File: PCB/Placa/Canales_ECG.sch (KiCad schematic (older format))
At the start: 39 parts, among them U1 INA333, U2 OPA2335, U3 OPA2335, U6 INA333, U7 OPA2335, U8 OPA2335

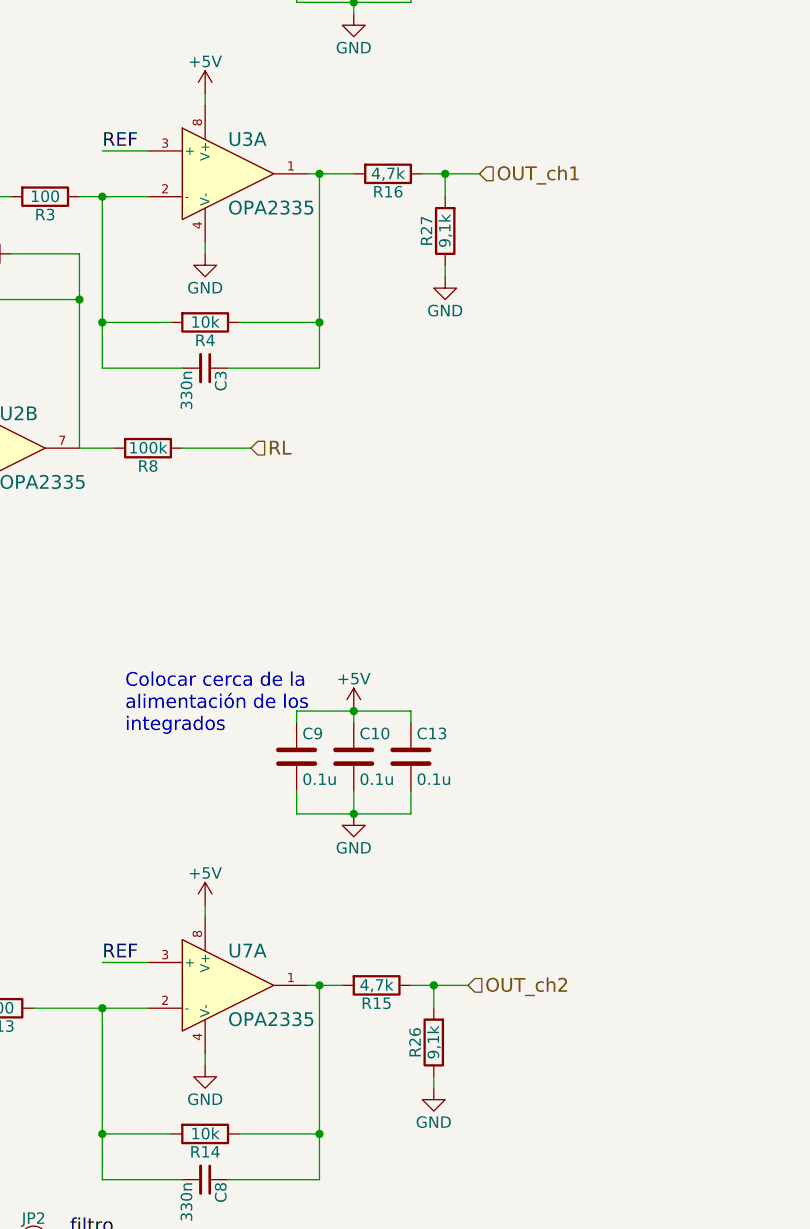
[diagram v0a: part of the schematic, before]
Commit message: Recalculé unas resistencias porque consigo de la serie E12
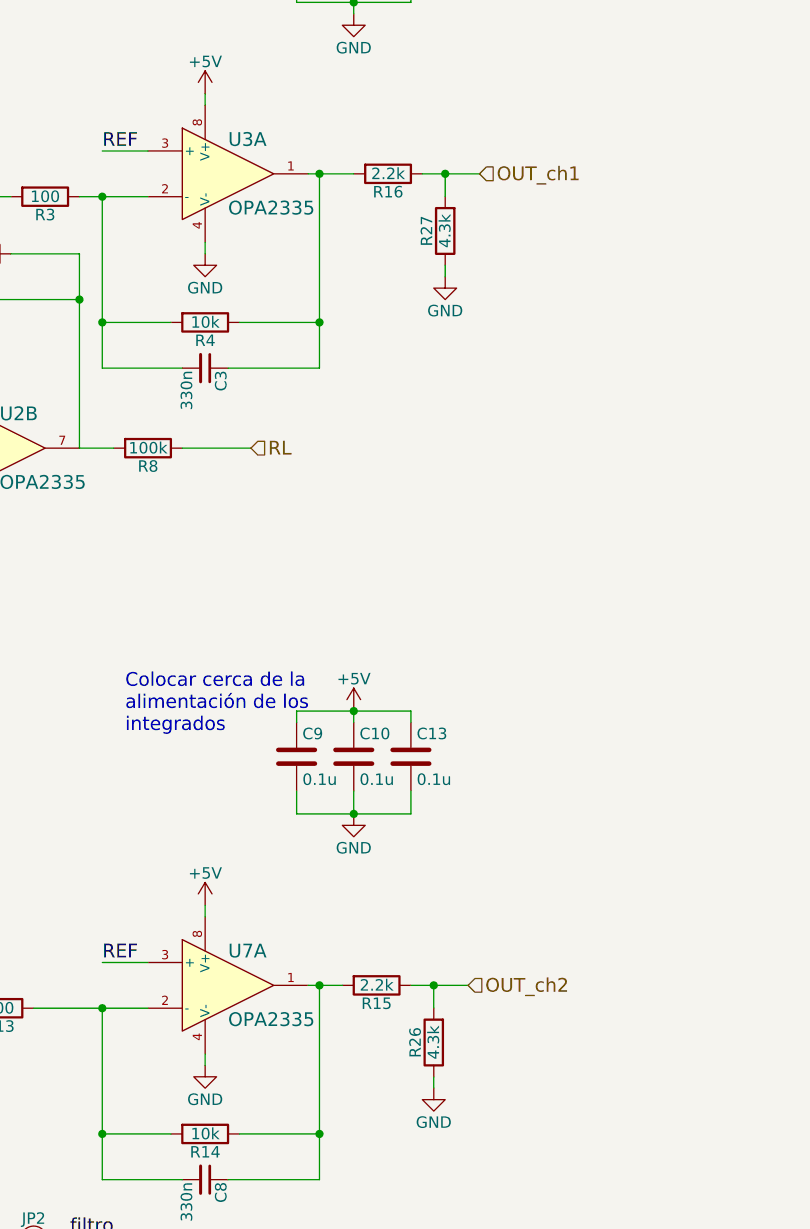
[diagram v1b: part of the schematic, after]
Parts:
- R15, R16: value 4,7k -> 2.2k
- R26, R27: value 9,1k -> 4.3k
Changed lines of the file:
@@
 P 5550 2050
 F 0 "R16" V 5630 2050 50  0000 C CNN
-F 1 "4,7k" V 5550 2050 50  0000 C CNN
+F 1 "2.2k" V 5550 2050 50  0000 C CNN
 F 2 "Resistors_SMD:R_0805" V 5480 2050 30  0001 C CNN
 F 3 "" H 5550 2050 30  0000 C CNN
@@
 P 5800 2300
 F 0 "R27" V 5880 2300 50  0000 C CNN
-F 1 "9,1k" V 5800 2300 50  0000 C CNN
+F 1 "4.3k" V 5800 2300 50  0000 C CNN
 F 2 "Resistors_SMD:R_0805" V 5730 2300 30  0001 C CNN
 F 3 "" H 5800 2300 30  0000 C CNN
@@
 P 5500 5600
 F 0 "R15" V 5580 5600 50  0000 C CNN
-F 1 "4,7k" V 5500 5600 50  0000 C CNN
+F 1 "2.2k" V 5500 5600 50  0000 C CNN
 F 2 "Resistors_SMD:R_0805" V 5430 5600 30  0001 C CNN
 F 3 "" H 5500 5600 30  0000 C CNN
@@
 P 5750 5850
 F 0 "R26" V 5830 5850 50  0000 C CNN
-F 1 "9,1k" V 5750 5850 50  0000 C CNN
+F 1 "4.3k" V 5750 5850 50  0000 C CNN
 F 2 "Resistors_SMD:R_0805" V 5680 5850 30  0001 C CNN
 F 3 "" H 5750 5850 30  0000 C CNN

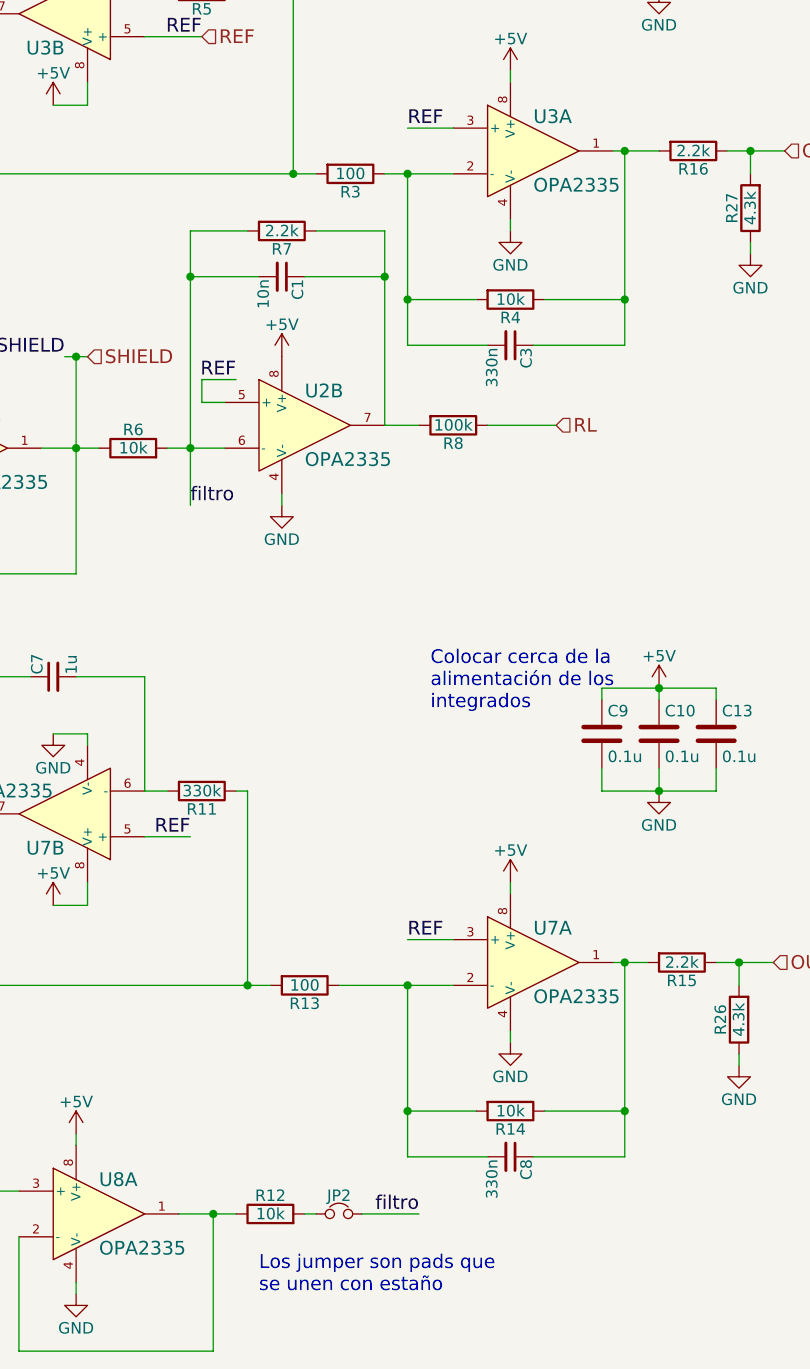
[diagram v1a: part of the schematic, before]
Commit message: Agrego el modelo 3D del cabezal con las tuercas. Modifico los valores de los componentes del amplificador de la salida de los canales del ECG.
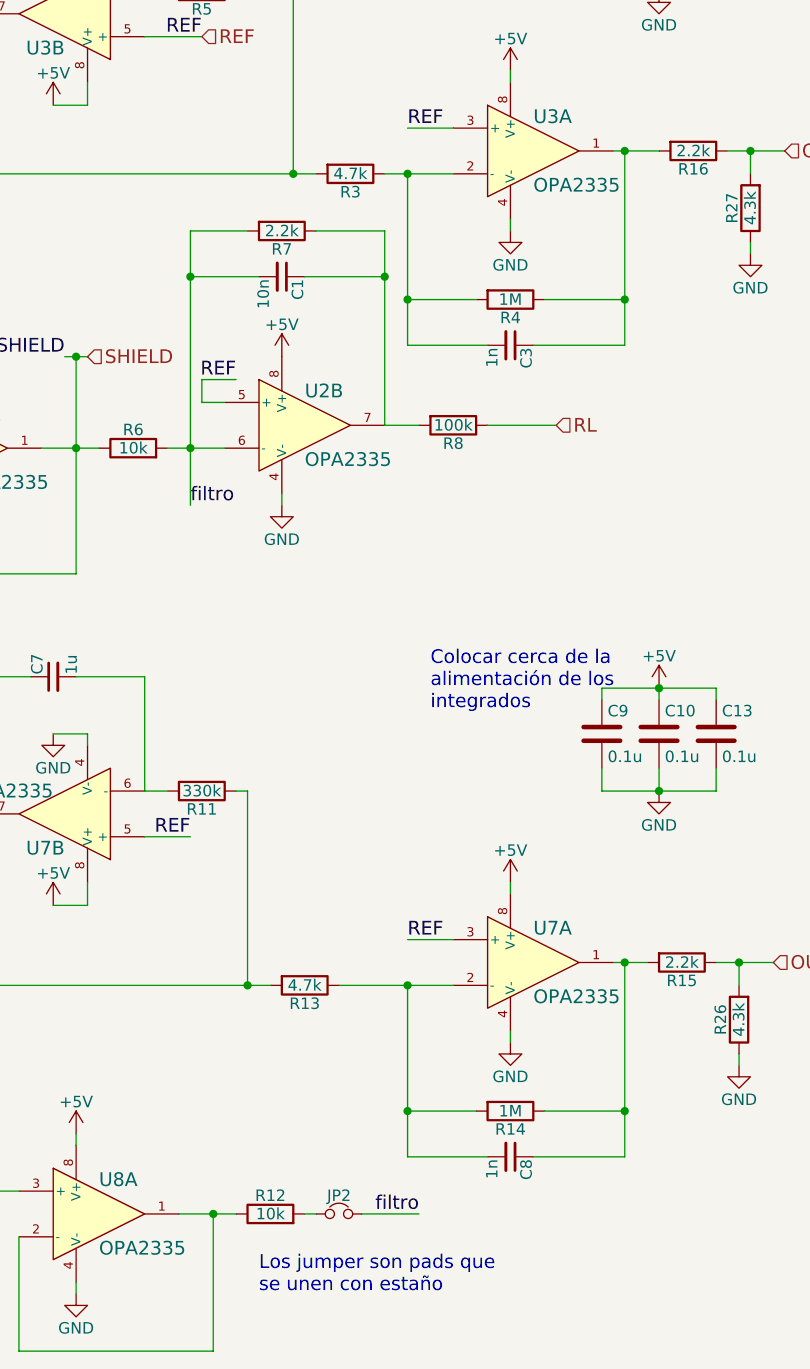
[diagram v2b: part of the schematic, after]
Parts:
- C3, C8: value 330n -> 1n
- R13, R3: value 100 -> 4.7k
- R14, R4: value 10k -> 1M
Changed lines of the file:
@@
 P 4050 2150
 F 0 "R3" V 4130 2150 50  0000 C CNN
-F 1 "100" V 4050 2150 50  0000 C CNN
+F 1 "4.7k" V 4050 2150 50  0000 C CNN
 F 2 "Resistors_SMD:R_0805" V 3980 2150 30  0001 C CNN
 F 3 "" H 4050 2150 30  0000 C CNN
@@
 P 4750 2700
 F 0 "R4" V 4830 2700 50  0000 C CNN
-F 1 "10k" V 4750 2700 50  0000 C CNN
+F 1 "1M" V 4750 2700 50  0000 C CNN
 F 2 "Resistors_SMD:R_0805" V 4680 2700 30  0001 C CNN
 F 3 "" H 4750 2700 30  0000 C CNN
@@
 P 4750 2900
 F 0 "C3" H 4760 2970 50  0000 L CNN
-F 1 "330n" H 4760 2820 50  0000 L CNN
+F 1 "1n" H 4760 2820 50  0000 L CNN
 F 2 "Capacitors_SMD:C_0805" H 4750 2900 60  0001 C CNN
 F 3 "" H 4750 2900 60  0000 C CNN
@@
 P 3850 5700
 F 0 "R13" V 3930 5700 50  0000 C CNN
-F 1 "100" V 3850 5700 50  0000 C CNN
+F 1 "4.7k" V 3850 5700 50  0000 C CNN
 F 2 "Resistors_SMD:R_0805" V 3780 5700 30  0001 C CNN
 F 3 "" H 3850 5700 30  0000 C CNN
@@
 P 4750 6250
 F 0 "R14" V 4830 6250 50  0000 C CNN
-F 1 "10k" V 4750 6250 50  0000 C CNN
+F 1 "1M" V 4750 6250 50  0000 C CNN
 F 2 "Resistors_SMD:R_0805" V 4680 6250 30  0001 C CNN
 F 3 "" H 4750 6250 30  0000 C CNN
@@
 P 4750 6450
 F 0 "C8" H 4760 6520 50  0000 L CNN
-F 1 "330n" H 4760 6370 50  0000 L CNN
+F 1 "1n" H 4760 6370 50  0000 L CNN
 F 2 "Capacitors_SMD:C_0805" H 4750 6450 60  0001 C CNN
 F 3 "" H 4750 6450 60  0000 C CNN
